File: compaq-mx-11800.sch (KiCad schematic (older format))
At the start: 245 parts, among them J1 Conn_01x16_Female, J2 Conn_01x16_Female

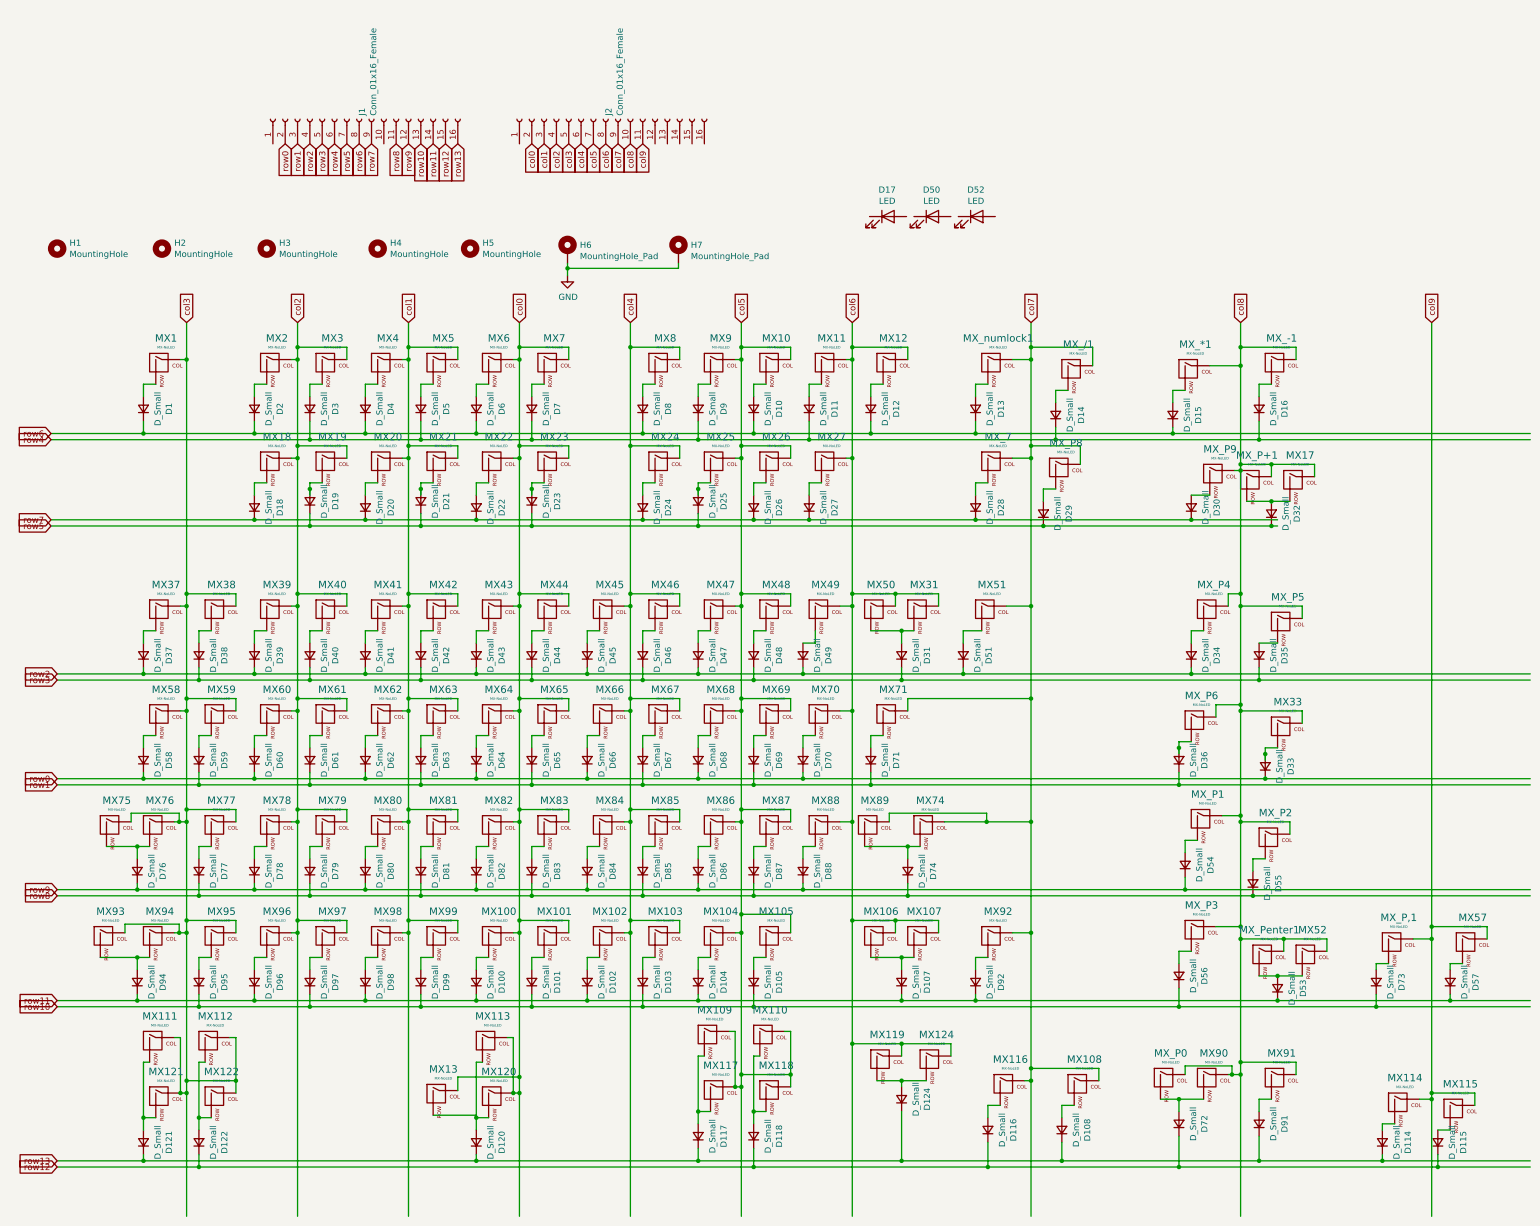
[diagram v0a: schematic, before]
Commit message: reorder keys and remove 1 column
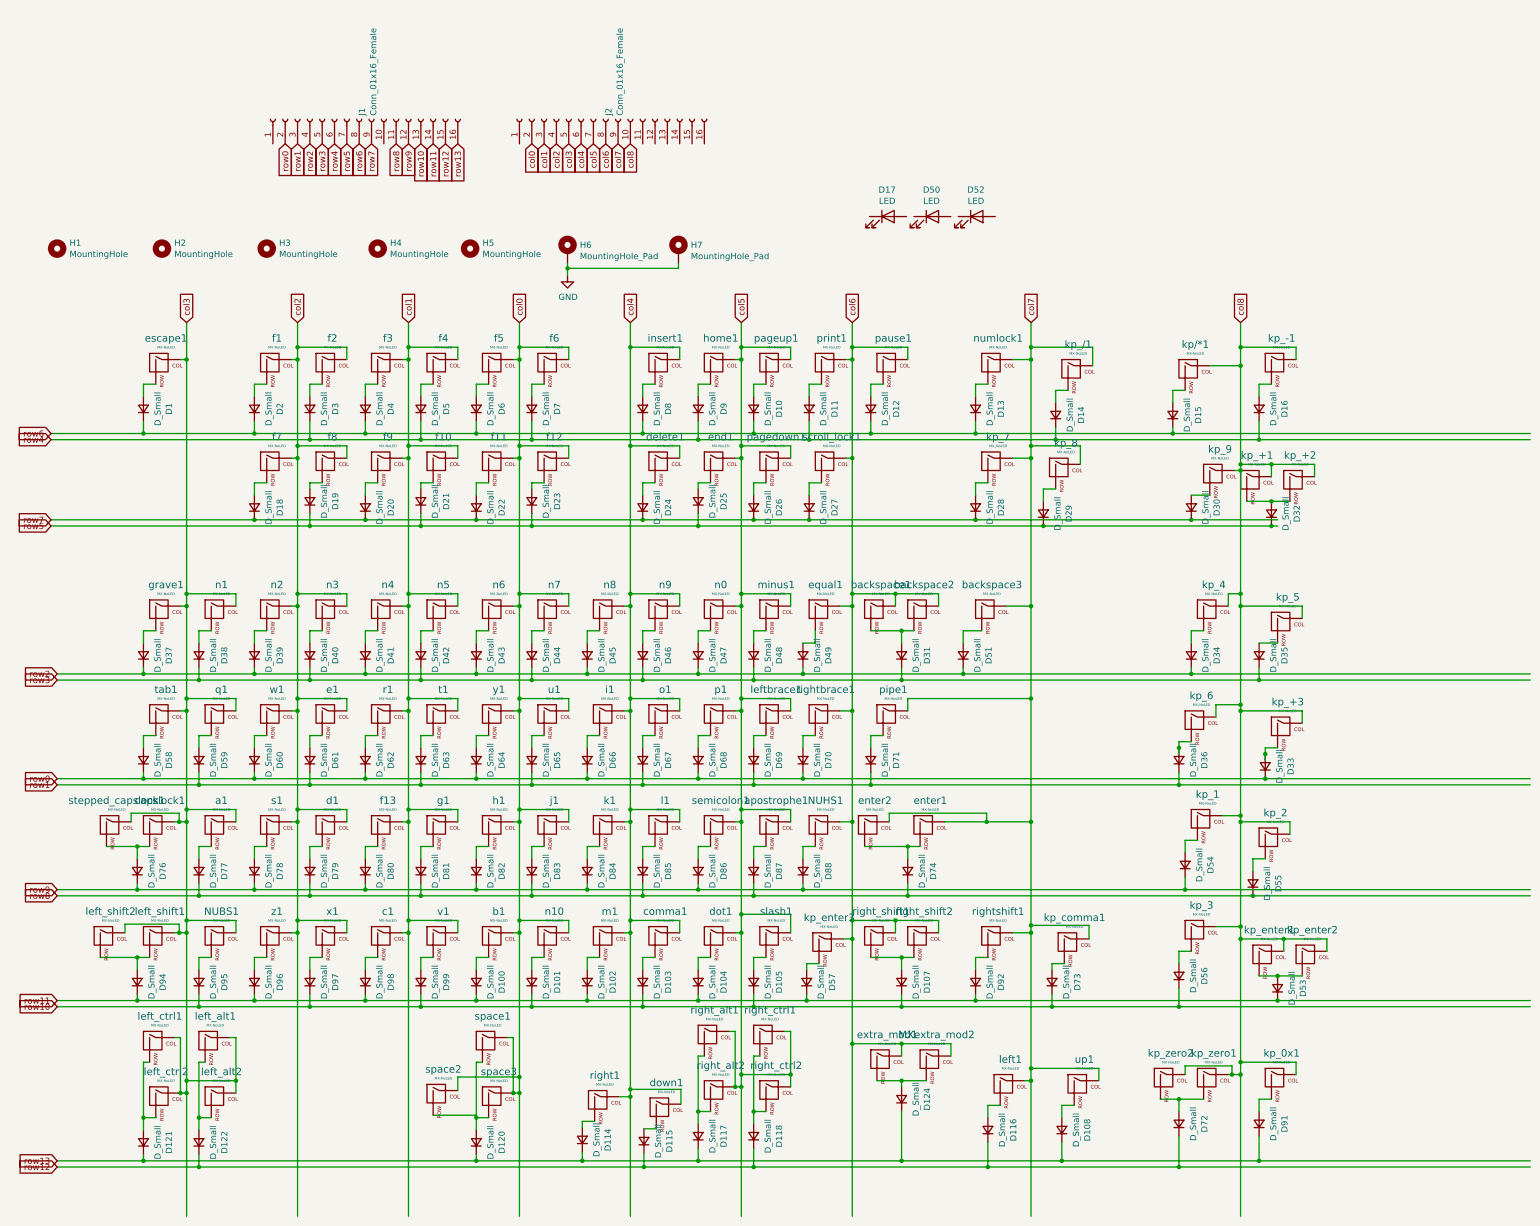
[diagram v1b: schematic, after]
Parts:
- kp_7: renamed from MX_7; value MX-NoLED -> MX_NoLED
- renumbered MX124 to MXextra_mod2, MX95 to NUBS1, MX88 to NUHS1, MX77 to a1, MX87 to apostrophe1, MX100 to b1, MX50 to backspace1, MX31 to backspace2, MX51 to backspace3, MX98 to c1, MX76 to capslock1, MX103 to comma1, MX79 to d1, MX24 to delete1, MX104 to dot1, MX115 to down1, MX61 to e1, MX25 to end1, MX74 to enter1, MX89 to enter2, MX49 to equal1, MX1 to escape1, MX119 to extra_mod1, MX2 to f1, MX21 to f10, MX22 to f11, MX23 to f12, MX80 to f13, MX3 to f2, MX4 to f3, MX5 to f4, MX6 to f5, MX7 to f6, MX18 to f7, MX19 to f8, MX20 to f9, MX81 to g1, MX37 to grave1, MX82 to h1, MX9 to home1, MX66 to i1, MX8 to insert1, MX83 to j1, MX84 to k1, MX_*1 to kp/*1, MX_P+1 to kp_+1, MX17 to kp_+2, MX33 to kp_+3, MX_-1 to kp_-1, MX_/1 to kp_/1, MX91 to kp_0x1, MX_P1 to kp_1, MX_P2 to kp_2, MX_P3 to kp_3, MX_P4 to kp_4, MX_P5 to kp_5, MX_P6 to kp_6, MX_P8 to kp_8, MX_P9 to kp_9, MX_P,1 to kp_comma1, MX_Penter1 to kp_enter1, MX52 to kp_enter2, MX57 to kp_enter3, MX90 to kp_zero1, MX_P0 to kp_zero2, MX85 to l1, MX116 to left1, MX112 to left_alt1, MX122 to left_alt2, MX111 to left_ctrl1, MX121 to left_ctrl2, MX94 to left_shift1, MX93 to left_shift2, MX69 to leftbrace1, MX102 to m1, MX48 to minus1, MX47 to n0, MX38 to n1, MX101 to n10, MX39 to n2, MX40 to n3, MX41 to n4, MX42 to n5, MX43 to n6, MX44 to n7, MX45 to n8, MX46 to n9, MX_numlock1 to numlock1, MX67 to o1, MX68 to p1, MX26 to pagedown1, MX10 to pageup1, MX12 to pause1, MX71 to pipe1, MX11 to print1, MX59 to q1, MX62 to r1, MX114 to right1, MX109 to right_alt1, MX117 to right_alt2, MX110 to right_ctrl1, MX118 to right_ctrl2, MX106 to right_shift1, MX107 to right_shift2, MX70 to rightbrace1, MX92 to rightshift1, MX78 to s1, MX27 to scroll_lock1, MX86 to semicolon1, MX105 to slash1, MX113 to space1, MX13 to space2, MX120 to space3, MX75 to stepped_capslock1, MX63 to t1, MX58 to tab1, MX65 to u1, MX108 to up1, MX99 to v1, MX60 to w1, MX97 to x1, MX64 to y1, MX96 to z1
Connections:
- net labels removed: col9
- wire segments 785 -> 780
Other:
- moved on the sheet: D114, D115, D57, D73, down1, kp_comma1, kp_enter3, right1

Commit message: modify bottom row
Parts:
- removed MXextra_mod2, left_alt2, left_ctrl2: MX-NoLED, MX_Only:MXOnly-1U-NoLED, symbol MX_Alps_Hybrid:MX-NoLED
- added D75: D_Small, Keebio-Parts:Diode-dual, symbol Device:D_Small
- added L_mod1_alt1, L_mod2_alt1, L_mod3: MX-NoLED, MX_Alps_Hybrid:MX-1.25U-NoLED, symbol MX_Alps_Hybrid:MX-NoLED
- L_mod1: renamed from left_ctrl1; footprint MX_Only:MXOnly-1.5U-NoLED -> MX_Alps_Hybrid:MX-1.5U-NoLED
- L_mod2: renamed from left_alt1; footprint MX_Only:MXOnly-1.5U-NoLED -> MX_Alps_Hybrid:MX-1.5U-NoLED
- R_mod1: renamed from right_alt2; footprint MX_Only:MXOnly-1.25U-NoLED -> MX_Alps_Hybrid:MX-1.25U-NoLED
- R_mod2: renamed from right_alt1; footprint MX_Only:MXOnly-1.5U-NoLED -> MX_Alps_Hybrid:MX-1.5U-NoLED
- R_mod2_alt1: renamed from right_ctrl2; footprint MX_Only:MXOnly-1.25U-NoLED -> MX_Alps_Hybrid:MX-1.25U-NoLED
- R_mod3: renamed from right_ctrl1; footprint MX_Only:MXOnly-1.5U-NoLED -> MX_Alps_Hybrid:MX-1.5U-NoLED
- R_mod3_alt1: renamed from extra_mod1; footprint MX_Only:MXOnly-1.25U-NoLED -> MX_Alps_Hybrid:MX-1.25U-NoLED
- space1: footprint MX_Only:MXOnly-7U-NoLED -> MX_Alps_Hybrid:MX-7U-NoLED
- space2: footprint MX_Only:MXOnly-7U-NoLED -> MX_Alps_Hybrid:MX-6.25U-NoLED
- space3: footprint MX_Only:MXOnly-6.25U-NoLED -> MX_Alps_Hybrid:MX-6.25U-NoLED
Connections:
- wire segments 780 -> 788
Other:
- moved on the sheet: D124, R_mod2, R_mod3, R_mod3_alt1

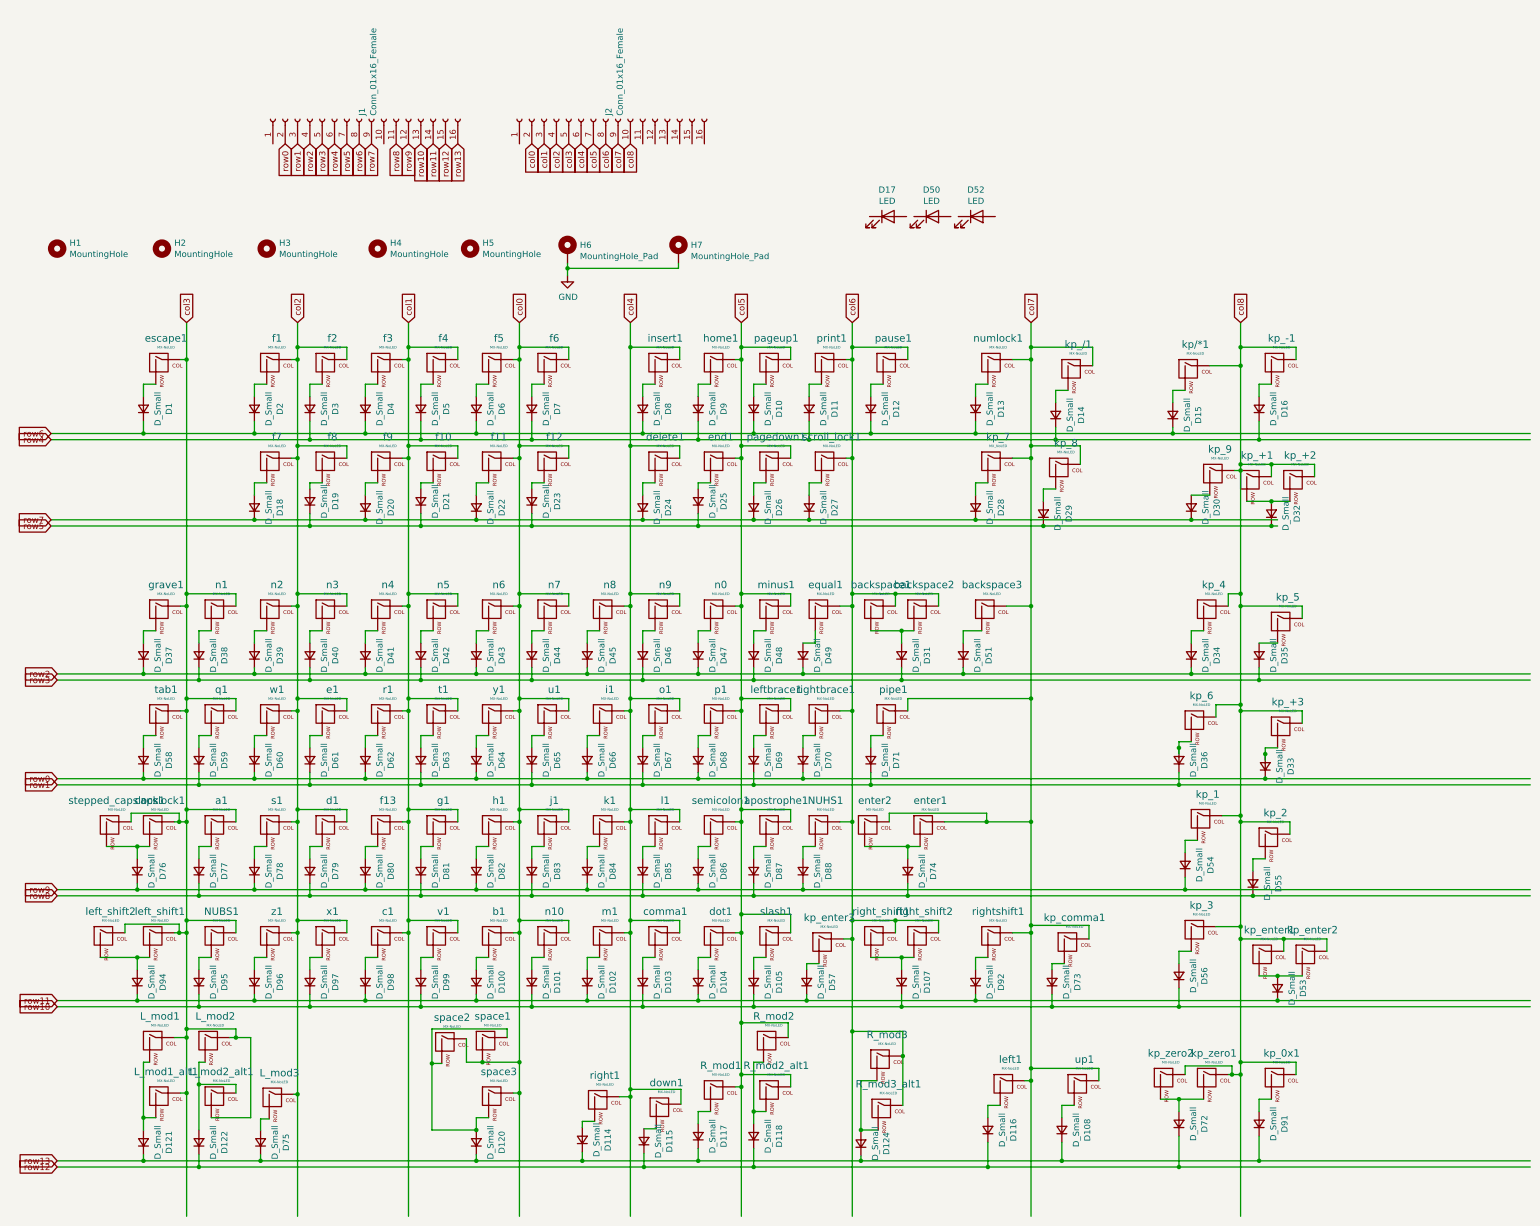
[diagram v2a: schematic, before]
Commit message: reorder columns and rows in schema and pcb to be in order
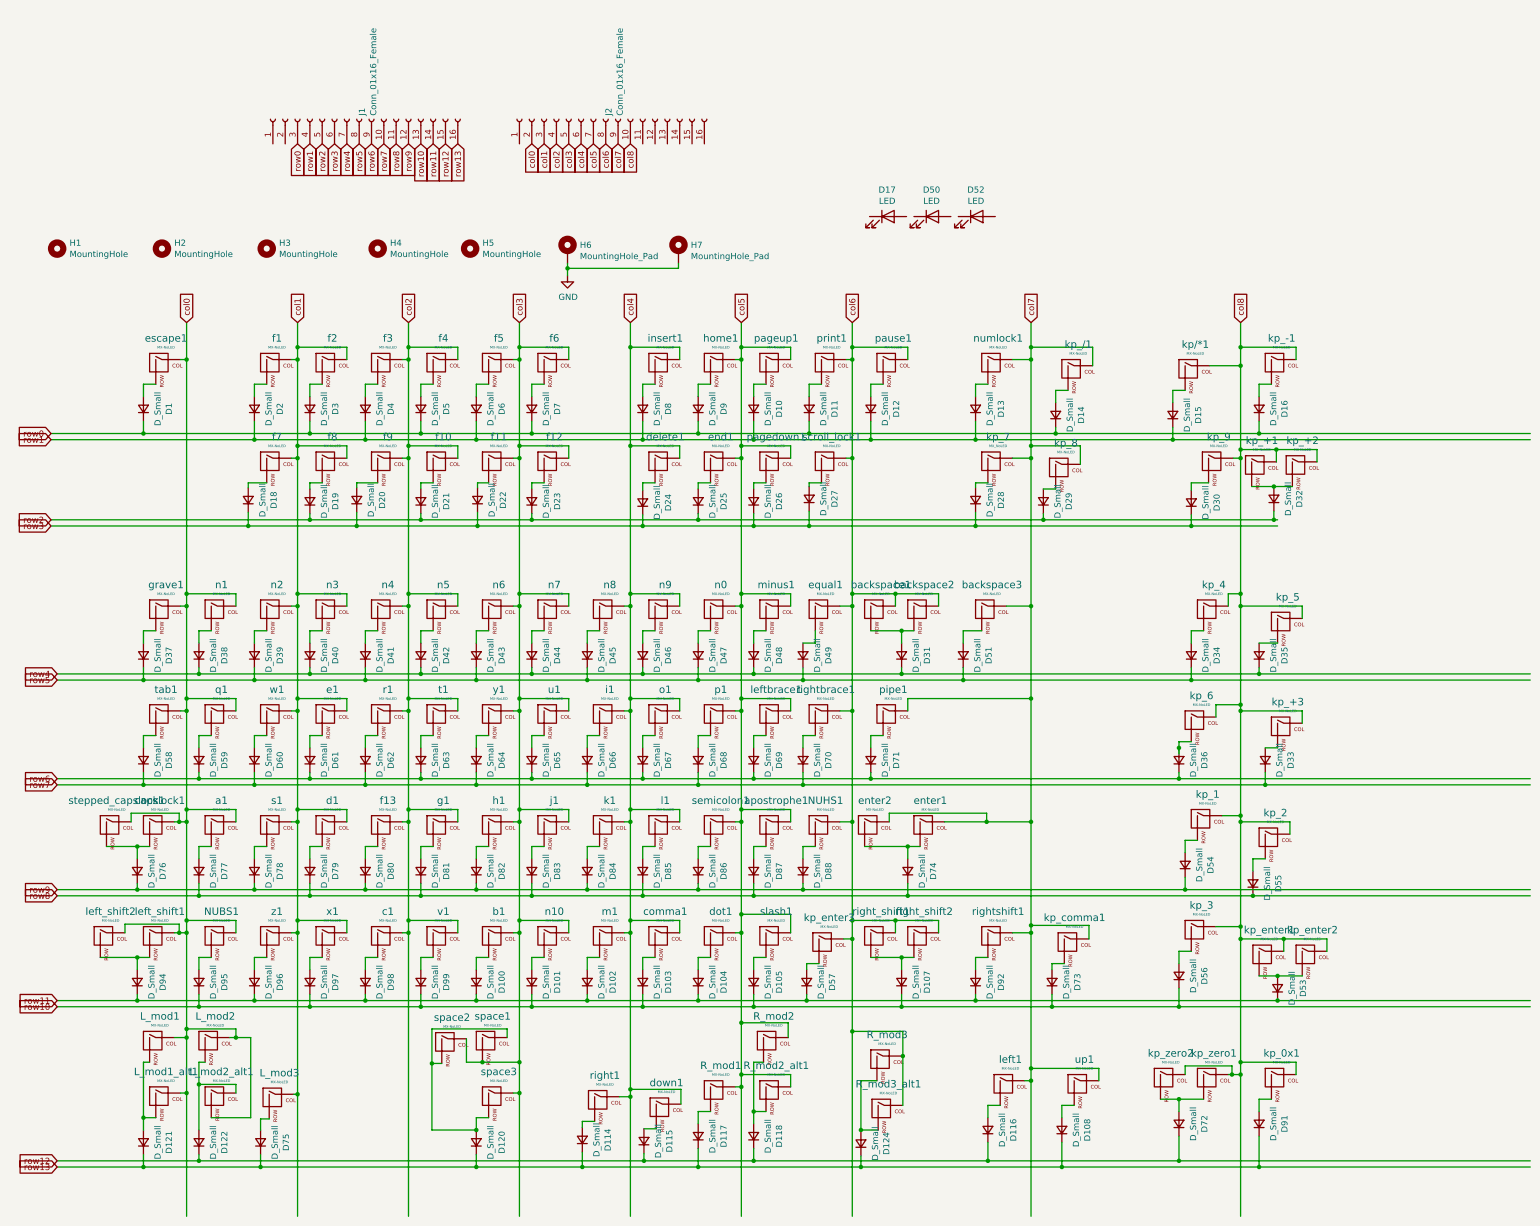
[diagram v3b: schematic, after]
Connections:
- wire segments 788 -> 797
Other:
- moved on the sheet: D18, D20, D22, D24, D26, D27, D28, D29, D30, D32, D33, kp_+1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
